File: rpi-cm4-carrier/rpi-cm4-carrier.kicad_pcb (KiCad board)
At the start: 2 copper layers, 40 x 55 mm, 25 parts, among them J1 USB4105-GF-A, U1 74LVC1G07QW5-7, U2 TPD4EUSB30, U3 D3V3F4U10LP-7, U4 BD2233G-GTR, U6 D3V3F4U10LP-7

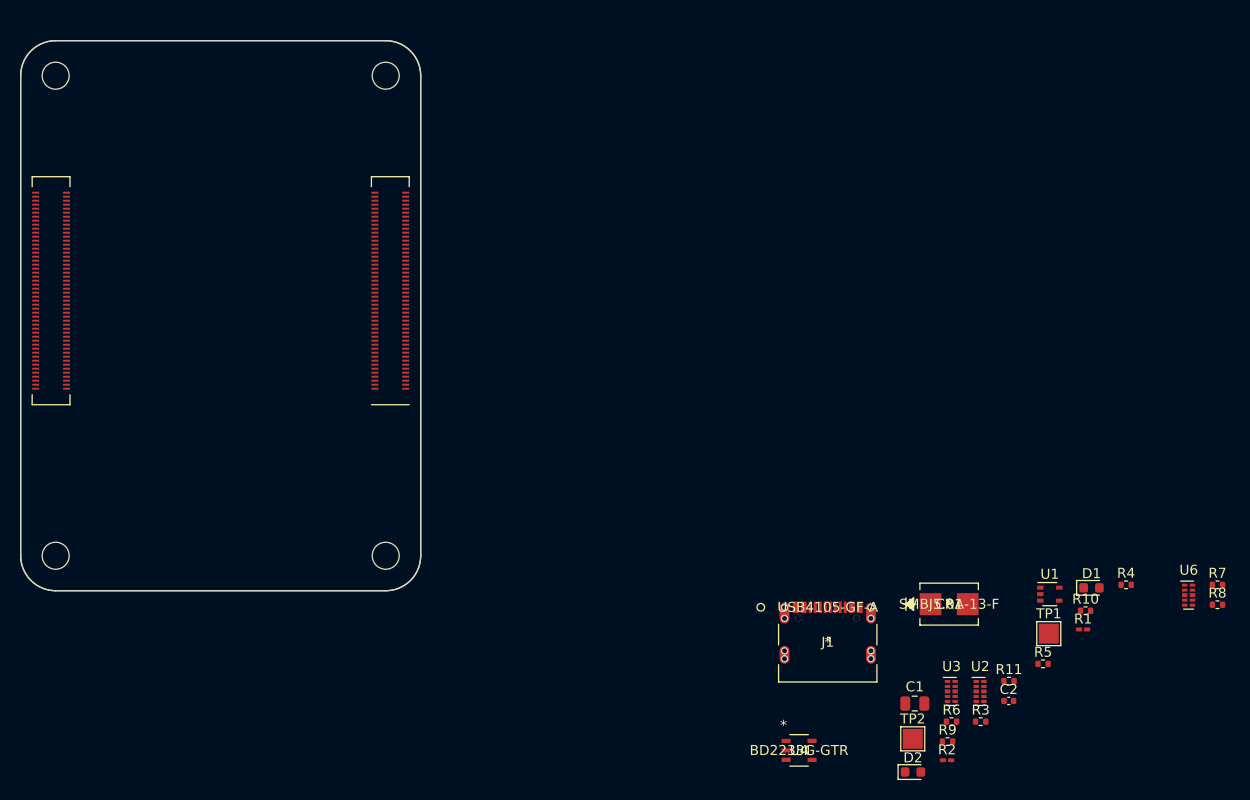
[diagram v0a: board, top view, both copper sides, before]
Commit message: Wired Ethernet data
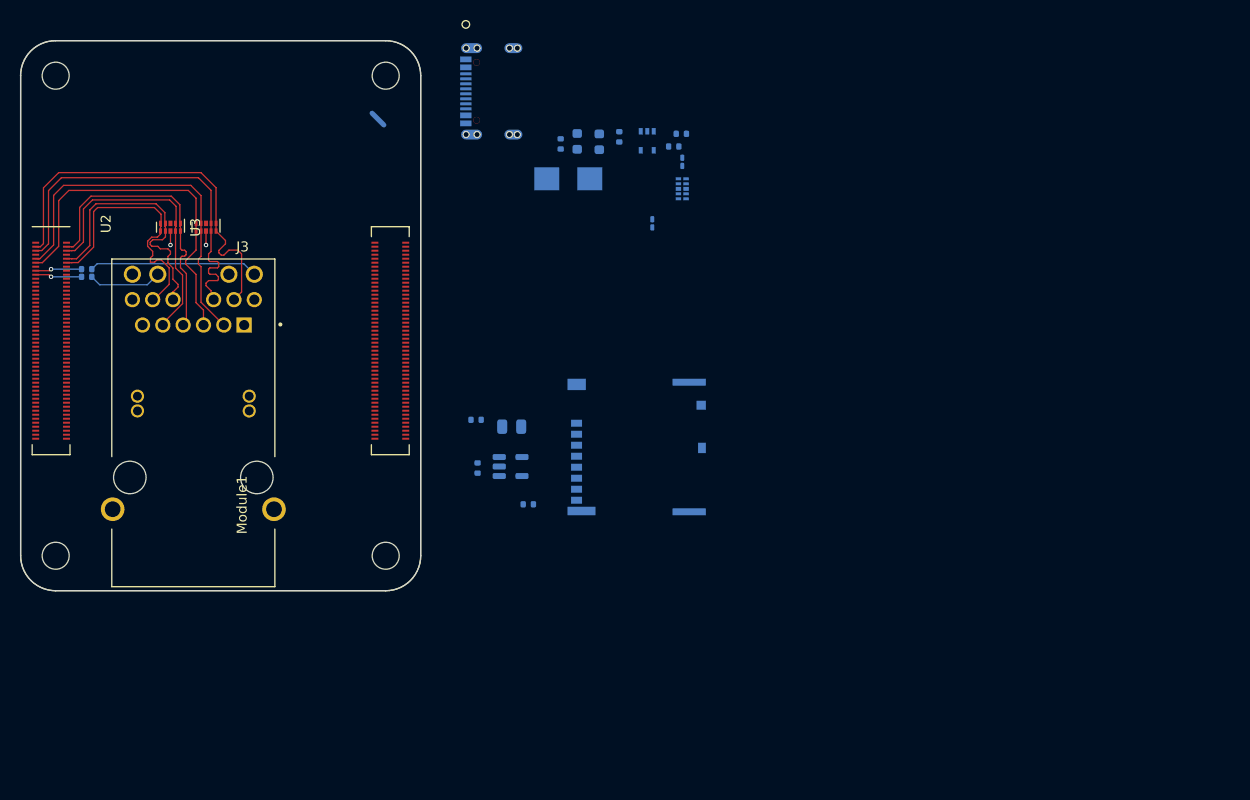
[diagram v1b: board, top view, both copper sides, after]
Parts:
- removed C2: 100n, Capacitor_SMD:C_0402_1005Metric
- removed TP1, TP2: TestPoint, TestPoint:TestPoint_Pad_2.0x2.0mm
- added J2: Micro_SD_Card_Det, CM4IO:SDCARD_MOLEX_503398-1892, B.Cu at (187.7, 119.1)
- added J3: 0826-1X1T-M1-F, 0826-1X1T-M1-F:0826-1X1T-M1-F, F.Cu at (143.8, 122.2)
- C1, J1, R1, R10, R11, R2, R3, R4, R5, R6, R7, R8, R9, U1, U6: moved to B.Cu
- CR1: footprint SMBJ5.0A-13-F:SMBJ5.0A-13-F -> Diode_SMD:D_SMB; moved to B.Cu
- D1: value LED Green -> LED Red; moved to B.Cu
- D2: value LED Red -> LED Green; moved to B.Cu
- Module1: value ComputeModule4-CM4 -> ComputeModule4
- U2: value TPD4EUSB30 -> D3V3F4U10LP-7
- U4: footprint BD2233G-GTR:BD2233G-GTR -> Package_TO_SOT_SMD:SOT-23-5; moved to B.Cu
- moved R10 105.6 mm to (133.1, 101.3), turned to 180 degrees
- moved R9 97.8 mm to (133.1, 102.1), turned to 180 degrees
- moved U3 90.8 mm to (141.5, 97.2), turned to -90 degrees
- moved U2 90.2 mm to (145.0, 97.2), turned to -90 degrees
- moved R4 71.7 mm to (180.5, 88.8), turned to -90 degrees
- moved D2 71.4 mm to (182.1, 88.6), turned to -90 degrees
- moved R8 71.4 mm to (192.6, 87.8)
- moved R7 69.8 mm to (191.8, 89.1), turned to 180 degrees
- moved R3 68.7 mm to (186.4, 88.1), turned to 90 degrees
- moved D1 66.4 mm to (184.4, 88.6), turned to 90 degrees
- moved U6 64.9 mm to (192.7, 93.3)
- moved J1 64.0 mm to (174.5, 83.6), turned to -90 degrees
- moved R1 61.6 mm to (192.7, 90.6), turned to 90 degrees
- moved R2 61.2 mm to (189.7, 96.8), turned to -90 degrees
- moved U1 60.6 mm to (189.2, 88.5), turned to -90 degrees
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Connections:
- net /CM4 GPIO/SD_PWR renamed /CM4 Ethernet and SD card/SD_PWR
- D1 pad 2: /CM4 GPIO/+3.3v -> +3.3V
- D2 pad 2: /CM4 GPIO/+3.3v -> +3.3V
- J1 pad A6: unconnected-(J1-PadA6) -> /CM4 USB and LEDs/USBD_P
- J1 pad A7: unconnected-(J1-PadA7) -> /CM4 USB and LEDs/USBD_N
- J1 pad B4-A9: unconnected-(J1-PadB4-A9) -> Net-(J1-PadB4-A9)
- Module1 pad 10: unconnected-(Module1-Pad10) -> /CM4 Ethernet and SD card/TRD0_N
- Module1 pad 101: unconnected-(Module1-Pad101) -> /CM4 USB and LEDs/USB_OTG_ID
- Module1 pad 102: unconnected-(Module1-Pad102) -> GND
- Module1 pad 103: unconnected-(Module1-Pad103) -> /CM4 USB and LEDs/USBD_N
- Module1 pad 105: unconnected-(Module1-Pad105) -> /CM4 USB and LEDs/USBD_P
- Module1 pad 11: unconnected-(Module1-Pad11) -> /CM4 Ethernet and SD card/TRD2_P
- Module1 pad 119: GND -> unconnected-(Module1-Pad119)
- Module1 pad 12: unconnected-(Module1-Pad12) -> /CM4 Ethernet and SD card/TRD0_P
- Module1 pad 120: GND -> unconnected-(Module1-Pad120)
- Module1 pad 121: unconnected-(Module1-Pad121) -> /CM4 USB and LEDs/nLED_Activity
- Module1 pad 122: unconnected-(Module1-Pad122) -> GND
- Module1 pad 123: unconnected-(Module1-Pad123) -> GND
- Module1 pad 125: GND -> unconnected-(Module1-Pad125)
- Module1 pad 126: GND -> unconnected-(Module1-Pad126)
- Module1 pad 131: GND -> unconnected-(Module1-Pad131)
- Module1 pad 133: unconnected-(Module1-Pad133) -> GND
- Module1 pad 137: GND -> unconnected-(Module1-Pad137)
- Module1 pad 138: GND -> unconnected-(Module1-Pad138)
- Module1 pad 142: unconnected-(Module1-Pad142) -> GND
- Module1 pad 143: unconnected-(Module1-Pad143) -> GND
- Module1 pad 144: GND -> unconnected-(Module1-Pad144)
- Module1 pad 15: unconnected-(Module1-Pad15) -> /CM4 Ethernet and SD card/ETH_LEDY
- Module1 pad 150: GND -> unconnected-(Module1-Pad150)
- Module1 pad 153: unconnected-(Module1-Pad153) -> GND
- Module1 pad 155: GND -> unconnected-(Module1-Pad155)
- Module1 pad 156: GND -> unconnected-(Module1-Pad156)
- Module1 pad 159: unconnected-(Module1-Pad159) -> GND
- Module1 pad 160: unconnected-(Module1-Pad160) -> GND
- Module1 pad 161: GND -> unconnected-(Module1-Pad161)
- Module1 pad 162: GND -> unconnected-(Module1-Pad162)
- Module1 pad 165: unconnected-(Module1-Pad165) -> GND
- Module1 pad 166: unconnected-(Module1-Pad166) -> GND
- Module1 pad 167: GND -> unconnected-(Module1-Pad167)
- Module1 pad 168: GND -> unconnected-(Module1-Pad168)
- Module1 pad 17: unconnected-(Module1-Pad17) -> /CM4 Ethernet and SD card/ETH_LEDG
- Module1 pad 171: unconnected-(Module1-Pad171) -> GND
- Module1 pad 173: GND -> unconnected-(Module1-Pad173)
- Module1 pad 175: unconnected-(Module1-Pad175) -> /CM4 USB and LEDs/SD_PWR_ON
- Module1 pad 176: unconnected-(Module1-Pad176) -> /CM4 USB and LEDs/Reserved
- Module1 pad 177: unconnected-(Module1-Pad177) -> +5V
- Module1 pad 179: GND -> +5V
- Module1 pad 180: GND -> unconnected-(Module1-Pad180)
- Module1 pad 181: unconnected-(Module1-Pad181) -> +5V
- Module1 pad 183: unconnected-(Module1-Pad183) -> +5V
- Module1 pad 184: unconnected-(Module1-Pad184) -> +3.3V
- Module1 pad 185: GND -> +5V
- Module1 pad 186: GND -> +3.3V
- Module1 pad 187: unconnected-(Module1-Pad187) -> +5V
- Module1 pad 188: unconnected-(Module1-Pad188) -> /CM4 USB and LEDs/+1.8V
- Module1 pad 190: unconnected-(Module1-Pad190) -> /CM4 USB and LEDs/+1.8V
- Module1 pad 191: GND -> unconnected-(Module1-Pad191)
- Module1 pad 192: GND -> unconnected-(Module1-Pad192)
- Module1 pad 195: unconnected-(Module1-Pad195) -> /CM4 USB and LEDs/nPWR_LED
- Module1 pad 197: GND -> unconnected-(Module1-Pad197)
- Module1 pad 21: /CM4 GPIO/nLED_Activity -> /CM4 Ethernet and SD card/nLED_Activity
- Module1 pad 3: unconnected-(Module1-Pad3) -> /CM4 Ethernet and SD card/TRD3_P
- Module1 pad 4: unconnected-(Module1-Pad4) -> /CM4 Ethernet and SD card/TRD1_P
- Module1 pad 5: unconnected-(Module1-Pad5) -> /CM4 Ethernet and SD card/TRD3_N
- Module1 pad 57: unconnected-(Module1-Pad57) -> /CM4 Ethernet and SD card/SD_CLK
- Module1 pad 6: unconnected-(Module1-Pad6) -> /CM4 Ethernet and SD card/TRD1_N
- Module1 pad 61: unconnected-(Module1-Pad61) -> /CM4 Ethernet and SD card/SD_DAT3
- Module1 pad 62: unconnected-(Module1-Pad62) -> /CM4 Ethernet and SD card/SD_CMD
- Module1 pad 63: unconnected-(Module1-Pad63) -> /CM4 Ethernet and SD card/SD_DAT0
- Module1 pad 67: unconnected-(Module1-Pad67) -> /CM4 Ethernet and SD card/SD_DAT1
- Module1 pad 69: unconnected-(Module1-Pad69) -> /CM4 Ethernet and SD card/SD_DAT2
- Module1 pad 75: unconnected-(Module1-Pad75) -> /CM4 Ethernet and SD card/SD_PWR_ON
- Module1 pad 76: unconnected-(Module1-Pad76) -> /CM4 Ethernet and SD card/Reserved
- Module1 pad 9: unconnected-(Module1-Pad9) -> /CM4 Ethernet and SD card/TRD2_N
- Module1 pad 95: /CM4 GPIO/nPWR_LED -> /CM4 Ethernet and SD card/nPWR_LED
- R10 pad 2: /CM4 GPIO/ETH_LEDY -> /CM4 Ethernet and SD card/ETH_LEDY
- R11 pad 1: /CM4 GPIO/+3.3v -> +3.3V
- R11 pad 2: /CM4 GPIO/SD_PWR_ON -> /CM4 Ethernet and SD card/SD_PWR_ON
- R3 pad 2: /CM4 GPIO/nLED_Activity -> Net-(R3-Pad2)
- R4 pad 2: Net-(R4-Pad2) -> /CM4 USB and LEDs/nLED_Activity
- R5 pad 1: /CM4 GPIO/+3.3v -> +3.3V
- R6 pad 1: /CM4 GPIO/Reserved -> /CM4 Ethernet and SD card/Reserved
- R7 pad 1: Net-(J4-Pad1) -> Net-(J1-PadB4-A9)
- R7 pad 2: /CM4 High Speed/USBOTG -> /CM4 USB and LEDs/USB_OTG_ID
- R8 pad 1: /CM4 High Speed/USBOTG -> /CM4 USB and LEDs/USB_OTG_ID
- R9 pad 2: /CM4 GPIO/ETH_LEDG -> /CM4 Ethernet and SD card/ETH_LEDG
- U1 pad 1: (no net) -> unconnected-(U1-Pad1)
- U1 pad 2: /CM4 GPIO/nPWR_LED -> /CM4 USB and LEDs/nPWR_LED
- U1 pad 4: Net-(R4-Pad2) -> Net-(R3-Pad2)
- U1 pad 5: /CM4 GPIO/+3.3v -> +3.3V
- U2 pad 1: /CM4 GPIO/TRD3_P -> /CM4 Ethernet and SD card/TRD3_P
- U2 pad 10: /CM4 GPIO/TRD3_P -> /CM4 Ethernet and SD card/TRD3_P
- U2 pad 2: /CM4 GPIO/TRD3_N -> /CM4 Ethernet and SD card/TRD3_N
- U2 pad 4: /CM4 GPIO/TRD2_N -> /CM4 Ethernet and SD card/TRD2_N
- U2 pad 5: /CM4 GPIO/TRD2_P -> /CM4 Ethernet and SD card/TRD2_P
- U2 pad 6: /CM4 GPIO/TRD2_P -> /CM4 Ethernet and SD card/TRD2_P
- U2 pad 7: /CM4 GPIO/TRD2_N -> /CM4 Ethernet and SD card/TRD2_N
- U2 pad 9: /CM4 GPIO/TRD3_N -> /CM4 Ethernet and SD card/TRD3_N
- U3 pad 1: /CM4 GPIO/TRD1_P -> /CM4 Ethernet and SD card/TRD1_P
- U3 pad 10: /CM4 GPIO/TRD1_P -> /CM4 Ethernet and SD card/TRD1_P
- U3 pad 2: /CM4 GPIO/TRD1_N -> /CM4 Ethernet and SD card/TRD1_N
- U3 pad 4: /CM4 GPIO/TRD0_N -> /CM4 Ethernet and SD card/TRD0_N
- U3 pad 5: /CM4 GPIO/TRD0_P -> /CM4 Ethernet and SD card/TRD0_P
- U3 pad 6: /CM4 GPIO/TRD0_P -> /CM4 Ethernet and SD card/TRD0_P
- U3 pad 7: /CM4 GPIO/TRD0_N -> /CM4 Ethernet and SD card/TRD0_N
- U3 pad 9: /CM4 GPIO/TRD1_N -> /CM4 Ethernet and SD card/TRD1_N
- U4 pad 1: /CM4 GPIO/+3.3v -> +3.3V
- U4 pad 3: /CM4 GPIO/SD_PWR_ON -> /CM4 Ethernet and SD card/SD_PWR_ON
- U6 pad 4: /CM4 High Speed/USBD_N -> /CM4 USB and LEDs/USBD_N
- U6 pad 5: /CM4 High Speed/USBD_P -> /CM4 USB and LEDs/USBD_P
- U6 pad 6: /CM4 High Speed/USBD_P -> /CM4 USB and LEDs/USBD_P
- U6 pad 7: /CM4 High Speed/USBD_N -> /CM4 USB and LEDs/USBD_N
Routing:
- net /CM4 Ethernet and SD card/TRD3_P: track 0.00 -> 39.8 mm
- net /CM4 Ethernet and SD card/TRD3_N: track 0.00 -> 38.7 mm
- net /CM4 Ethernet and SD card/TRD2_N: track 0.00 -> 37.0 mm
- net /CM4 Ethernet and SD card/TRD2_P: track 0.00 -> 35.9 mm
- net /CM4 Ethernet and SD card/TRD1_P: track 0.00 -> 28.9 mm
- net /CM4 Ethernet and SD card/TRD1_N: track 0.00 -> 28.3 mm
- net /CM4 Ethernet and SD card/TRD0_N: track 0.00 -> 26.9 mm
- net /CM4 Ethernet and SD card/TRD0_P: track 0.00 -> 26.3 mm
- net Net-(J3-Pad17): track 0.00 -> 16.9 mm
- net Net-(J3-Pad19): track 0.00 -> 7.37 mm
- net /CM4 Ethernet and SD card/ETH_LEDG: track 0.00 -> 4.67 mm, vias 0 -> 1
- net /CM4 Ethernet and SD card/ETH_LEDY: track 0.00 -> 4.65 mm, vias 0 -> 1
- net GND: track 0.00 -> 4.46 mm, vias 0 -> 2
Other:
- board text removed: "RPi CM4 Carrier Template"
